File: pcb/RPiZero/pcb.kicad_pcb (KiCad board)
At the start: 2 copper layers, 87.5 x 62.5 mm, 10 parts, among them M1 Vibration Motor, SW1 M2011S3AW03, U1 TP4056

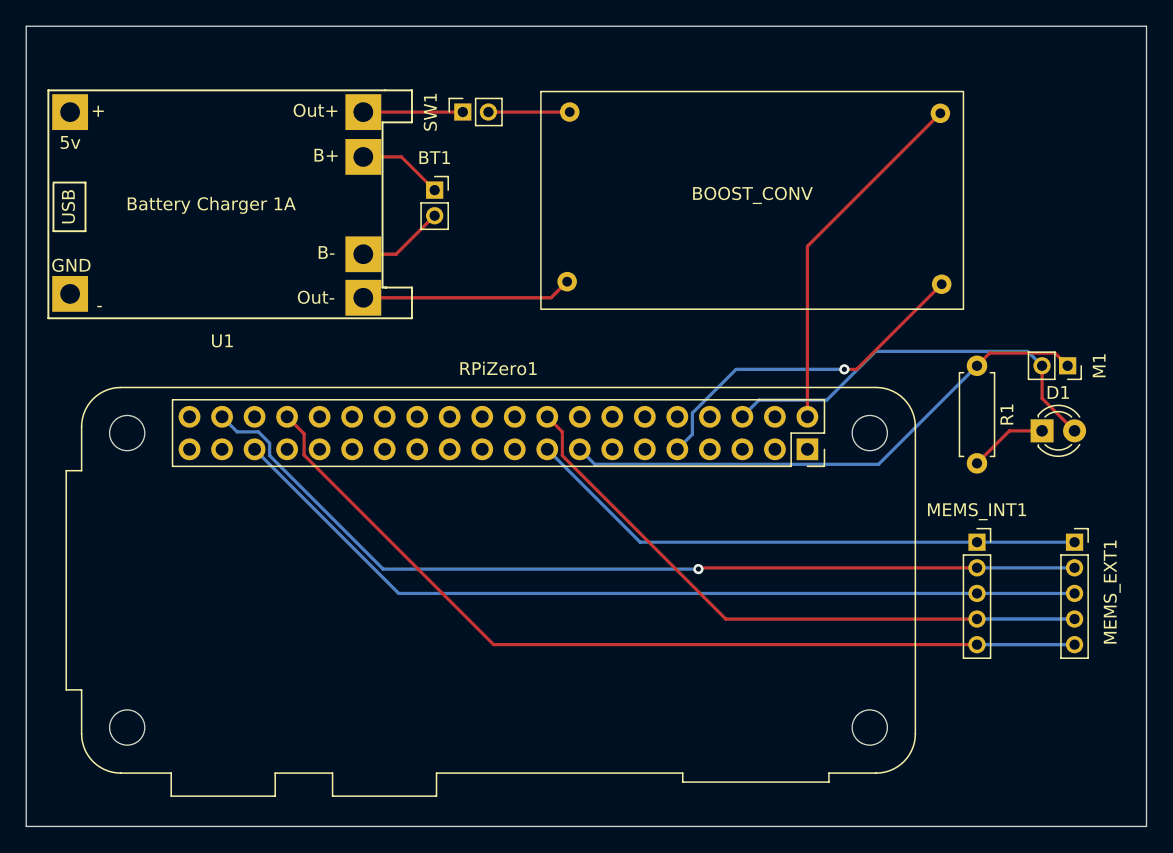
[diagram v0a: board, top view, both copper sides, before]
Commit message: Add new folder for ESP32 PCB
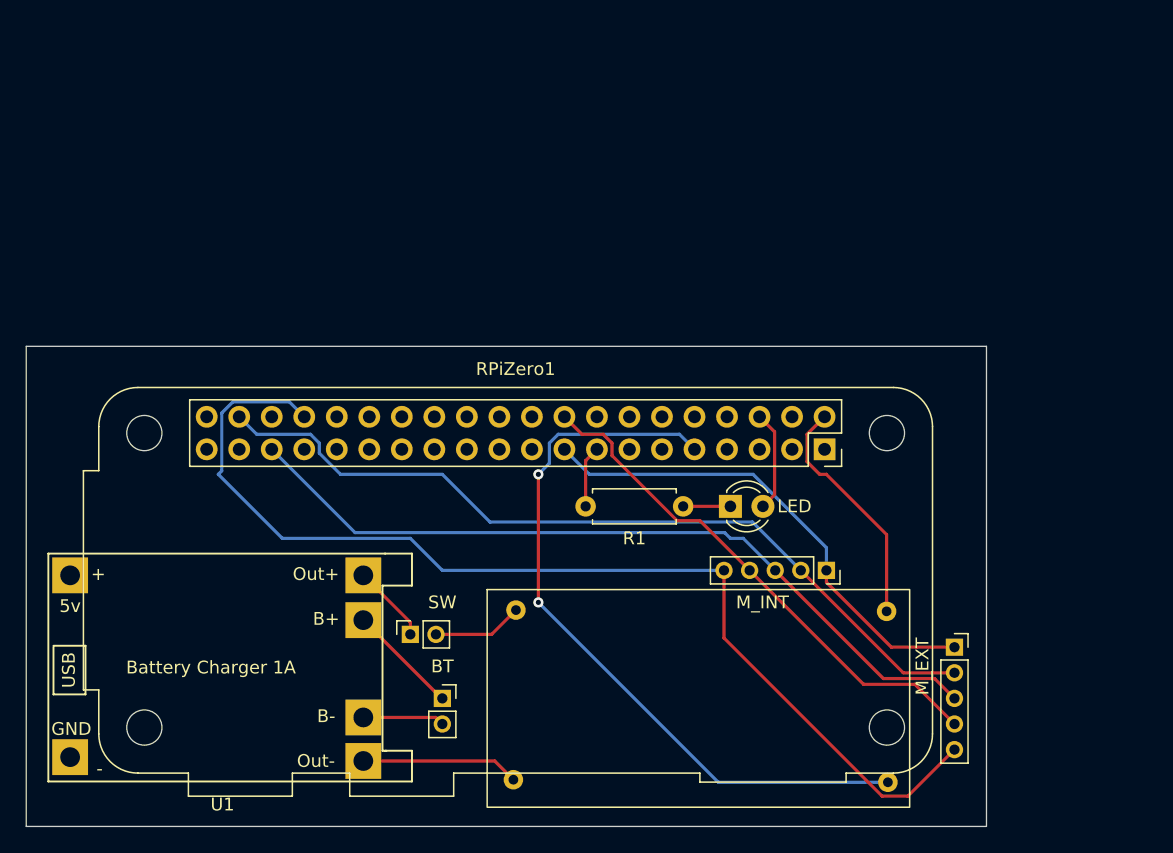
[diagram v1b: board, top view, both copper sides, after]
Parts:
- removed M1: Vibration Motor, Connector_PinSocket_2.00mm:PinSocket_1x02_P2.00mm_Vertical
- moved SW 41.0 mm to (67.5, 117.5)
- moved BT 39.7 mm to (70.0, 122.5)
- moved U 39.1 mm to (90.0, 122.5)
- moved U1 36.2 mm to (39.2, 111.2)
- moved R1 32.5 mm to (81.2, 107.5), turned to 0 degrees
- moved LED 25.0 mm to (92.5, 107.5)
- moved M_EXT 12.5 mm to (110.0, 118.5)
- moved M_INT 12.0 mm to (100.0, 112.5), turned to -90 degrees
- moved RPiZero1 1.34 mm to (99.9, 103.0)
- renumbered BT1 to BT, D1 to LED, MEMS_EXT1 to M_EXT, MEMS_INT1 to M_INT, SW1 to SW, BOOST_CONV to U
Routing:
- net Net-(R1-Pad1): track 42.6 -> 4.82 mm
- net Net-(RPiZero1-Pad9): track 27.0 -> 58.0 mm, vias 1 -> 2
- net Net-(D1-Pad2): track 32.1 -> 7.86 mm
- net Net-(MEMS_EXT1-Pad5): track 69.8 -> 84.7 mm
- net Net-(RPiZero1-Pad2): track 28.0 -> 18.6 mm
- net Net-(MEMS_EXT1-Pad4): track 48.8 -> 41.0 mm
- net Net-(MEMS_EXT1-Pad2): track 72.1 -> 64.6 mm, vias 1 -> 0
- net Net-(MEMS_EXT1-Pad3): track 68.7 -> 61.4 mm
- net Net-(MEMS_EXT1-Pad1): track 44.3 -> 38.4 mm
- net Net-(U1-Pad4): track 16.4 -> 12.3 mm
- net Net-(D1-Pad1): track 6.13 -> 3.69 mm
- net Net-(BT1-Pad1): track 6.65 -> 8.70 mm
- net Net-(SW1-Pad1): track 7.78 -> 6.13 mm
- net Net-(SW1-Pad2): track 6.35 -> 7.04 mm
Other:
- board size 87.5 x 62.5 mm -> 75 x 37.5 mm
